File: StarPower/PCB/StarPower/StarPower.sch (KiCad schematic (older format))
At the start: 13 parts, among them SW1 SW_Push, U1 ATtiny25-20SSU, U2 SGM809, U3 PAM2804AAB010, Y1 32768 Hz

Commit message: Set more part footprints.
The microcontroller is now directly connected to the battery.
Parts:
- C1: footprint (none) -> Capacitor_SMD:C_1206_3216Metric_Pad1.42x1.75mm_HandSolder
- C2: renamed from C5; footprint (none) -> Capacitor_SMD:C_1206_3216Metric_Pad1.42x1.75mm_HandSolder
- C3: footprint (none) -> Capacitor_SMD:C_0805_2012Metric_Pad1.18x1.45mm_HandSolder
- C4: renamed from C2; footprint (none) -> Capacitor_SMD:C_0805_2012Metric_Pad1.18x1.45mm_HandSolder
- C5: renamed from C4; footprint (none) -> Capacitor_SMD:C_0805_2012Metric_Pad1.18x1.45mm_HandSolder
- U2: value SGM809 -> SGM809B-SXN3LG; footprint (none) -> Package_TO_SOT_SMD:SOT-23W_Handsoldering
- Y1: value 32768 Hz -> 32.768 kHz; footprint (none) -> Crystal:Crystal_SMD_SeikoEpson_MC146-4Pin_6.7x1.5mm_HandSoldering
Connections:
- net +2V8: no longer U1.8 (VCC)
- net +BATT: now also U1.8 (VCC)
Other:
- note added: "Iled ~~ 122 mA"
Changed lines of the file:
@@
-$EndComp
-$Comp
-L Device:Crystal Y1
-U 1 1 6369D0A6
-P 4600 5350
-F 0 "Y1" V 4350 5350 50  0000 C CNN
-F 1 "32768 Hz" V 4850 5350 50  0000 C CNN
-F 2 "" H 4600 5350 50  0001 C CNN
-F 3 "~" H 4600 5350 50  0001 C CNN
-	1    4600 5350
-	0    1    1    0
 $EndComp
 $Comp
@@
 F 0 "C3" H 5465 5546 50  0000 L CNN
 F 1 "C" H 5465 5455 50  0000 L CNN
-F 2 "" H 5388 5350 50  0001 C CNN
+F 2 "Capacitor_SMD:C_0805_2012Metric_Pad1.18x1.45mm_HandSolder" H 5388 5350 50  0001 C CNN
 F 3 "~" H 5350 5500 50  0001 C CNN
 	1    5350 5500
@@
 $EndComp
 $Comp
-L Device:C C2
+L Device:C C4
 U 1 1 6369DFE7
 P 5350 5200
-F 0 "C2" H 5465 5246 50  0000 L CNN
+F 0 "C4" H 5465 5246 50  0000 L CNN
 F 1 "C" H 5465 5155 50  0000 L CNN
-F 2 "" H 5388 5050 50  0001 C CNN
+F 2 "Capacitor_SMD:C_0805_2012Metric_Pad1.18x1.45mm_HandSolder" H 5388 5050 50  0001 C CNN
 F 3 "~" H 5350 5200 50  0001 C CNN
 	1    5350 5200
@@
 $EndComp
 $Comp
-L Device:C C5
+L Device:C C2
 U 1 1 636A08B3
 P 8250 3100
-F 0 "C5" H 8365 3146 50  0000 L CNN
+F 0 "C2" H 8365 3146 50  0000 L CNN
 F 1 "C1206C106K3PACTU" H 8365 3055 50  0000 L CNN
-F 2 "" H 8288 2950 50  0001 C CNN
+F 2 "Capacitor_SMD:C_1206_3216Metric_Pad1.42x1.75mm_HandSolder" H 8288 2950 50  0001 C CNN
 F 3 "~" H 8250 3100 50  0001 C CNN
 	1    8250 3100
@@
 $EndComp
 $Comp
-L Device:C C4
+L Device:C C5
 U 1 1 636A0DE7
 P 7750 3100
-F 0 "C4" H 7865 3146 50  0000 L CNN
+F 0 "C5" H 7865 3146 50  0000 L CNN
 F 1 "100 nF" H 7865 3055 50  0000 L CNN
-F 2 "" H 7788 2950 50  0001 C CNN
+F 2 "Capacitor_SMD:C_0805_2012Metric_Pad1.18x1.45mm_HandSolder" H 7788 2950 50  0001 C CNN
 F 3 "~" H 7750 3100 50  0001 C CNN
 	1    7750 3100
@@
 P 3100 3150
 F 0 "U2" H 2870 3196 50  0000 R CNN
-F 1 "SGM809" H 2870 3105 50  0000 R CNN
-F 2 "" H 2700 3300 50  0001 C CNN
+F 1 "SGM809B-SXN3LG" H 2870 3105 50  0000 R CNN
+F 2 "Package_TO_SOT_SMD:SOT-23W_Handsoldering" H 2700 3300 50  0001 C CNN
 F 3 "http://www.sg-micro.com/uploads/soft/20190626/1561528457.pdf" H 2800 3400 50  0001 C CNN
 	1    3100 3150
@@
 F 0 "C1" H 4665 3246 50  0000 L CNN
 F 1 "C1206C106K3PACTU" H 4665 3155 50  0000 L CNN
-F 2 "" H 4588 3050 50  0001 C CNN
+F 2 "Capacitor_SMD:C_1206_3216Metric_Pad1.42x1.75mm_HandSolder" H 4588 3050 50  0001 C CNN
 F 3 "~" H 4550 3200 50  0001 C CNN
 F 4 "±10 %; X5R" H 4550 3200 50  0001 C CNN "Characteristics"
@@
 	8250 3600 8250 3250
 Wire Wire Line
-	6850 3100 6450 3100
-Wire Wire Line
-	6450 3100 6450 2900
-Wire Wire Line
-	6450 2900 6000 2900
+	6850 3100 6100 3100
+Wire Wire Line
+	6100 3100 6100 2900
+Wire Wire Line
+	6100 2900 6000 2900
 Connection ~ 6850 3100
 Wire Wire Line
@@
 $EndComp
 Connection ~ 8250 2700
-$Comp
-L power:+2V8 #PWR0106
-U 1 1 636E305D
-P 2800 4650
-F 0 "#PWR0106" H 2800 4500 50  0001 C CNN
-F 1 "+2V8" H 2815 4823 50  0000 C CNN
-F 2 "" H 2800 4650 50  0001 C CNN
-F 3 "" H 2800 4650 50  0001 C CNN
-	1    2800 4650
-	1    0    0    -1
-$EndComp
 Wire Wire Line
 	2800 4650 2800 4700
@@
 Text Notes 7250 3350 0    50   ~ 0
 0.82 Ω
+$Comp
+L power:+BATT #PWR0106
+U 1 1 636EEFD2
+P 2800 4650
+F 0 "#PWR0106" H 2800 4500 50  0001 C CNN
+F 1 "+BATT" H 2815 4823 50  0000 C CNN
+F 2 "" H 2800 4650 50  0001 C CNN
+F 3 "" H 2800 4650 50  0001 C CNN
+	1    2800 4650
+	1    0    0    -1
+$EndComp
+$Comp
+L Device:Crystal Y1
+U 1 1 6369D0A6
+P 4600 5350
+F 0 "Y1" V 4350 5350 50  0000 C CNN
+F 1 "32.768 kHz" V 4850 5350 50  0000 C CNN
+F 2 "Crystal:Crystal_SMD_SeikoEpson_MC146-4Pin_6.7x1.5mm_HandSoldering" H 4600 5350 50  0001 C CNN
+F 3 "~" H 4600 5350 50  0001 C CNN
+	1    4600 5350
+	0    1    1    0
+$EndComp
+Text Notes 7000 3100 0    50   ~ 0
+Iled ~~ 122 mA
 $EndSCHEMATC

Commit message: Add mounting holes and the correct footprint for the push button.
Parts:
- added H1, H2: MountingHole, MountingHole:MountingHole_3.5mm, symbol Mechanical:MountingHole
- added H3: MountingHole, MountingHole:MountingHole_2.5mm, symbol Mechanical:MountingHole
- SW1: value SW_Push -> TL3301; footprint (none) -> mibe:SW_SPST_TL3301
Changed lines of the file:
@@
 P 4000 5000
 F 0 "SW1" H 4000 5285 50  0000 C CNN
-F 1 "SW_Push" H 4000 5194 50  0000 C CNN
-F 2 "" H 4000 5200 50  0001 C CNN
+F 1 "TL3301" H 4000 5194 50  0000 C CNN
+F 2 "mibe:SW_SPST_TL3301" H 4000 5200 50  0001 C CNN
 F 3 "~" H 4000 5200 50  0001 C CNN
 	1    4000 5000
@@
 Text Notes 7000 3100 0    50   ~ 0
 Iled ~~ 122 mA
+$Comp
+L Mechanical:MountingHole H1
+U 1 1 6372BC7B
+P 7700 6000
+F 0 "H1" H 7800 6046 50  0000 L CNN
+F 1 "MountingHole" H 7800 5955 50  0000 L CNN
+F 2 "MountingHole:MountingHole_3.5mm" H 7700 6000 50  0001 C CNN
+F 3 "~" H 7700 6000 50  0001 C CNN
+	1    7700 6000
+	1    0    0    -1
+$EndComp
+$Comp
+L Mechanical:MountingHole H2
+U 1 1 6372C182
+P 8500 6000
+F 0 "H2" H 8600 6046 50  0000 L CNN
+F 1 "MountingHole" H 8600 5955 50  0000 L CNN
+F 2 "MountingHole:MountingHole_3.5mm" H 8500 6000 50  0001 C CNN
+F 3 "~" H 8500 6000 50  0001 C CNN
+	1    8500 6000
+	1    0    0    -1
+$EndComp
+$Comp
+L Mechanical:MountingHole H3
+U 1 1 6372C56E
+P 9300 6000
+F 0 "H3" H 9400 6046 50  0000 L CNN
+F 1 "MountingHole" H 9400 5955 50  0000 L CNN
+F 2 "MountingHole:MountingHole_2.5mm" H 9300 6000 50  0001 C CNN
+F 3 "~" H 9300 6000 50  0001 C CNN
+	1    9300 6000
+	1    0    0    -1
+$EndComp
 $EndSCHEMATC

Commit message: Named most nets.
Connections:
- net SW: now reaches L1.1, U3.3 (SW)
- net FB: now reaches D1.1 (K), R1.1, U3.5 (FB)
- net XTAL1: now reaches C4.2, U1.2 (XTAL1/PB3), Y1.1
- net XTAL2: now reaches C3.2, U1.3 (XTAL2/PB4), Y1.2
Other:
- moved on the sheet: L1
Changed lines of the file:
@@
-$EndComp
-$Comp
-L Device:L L1
-U 1 1 6369E4E0
-P 6450 2700
-F 0 "L1" V 6640 2700 50  0000 C CNN
-F 1 "SRU1038-150Y" V 6549 2700 50  0000 C CNN
-F 2 "Inductor_SMD:L_Bourns-SRU1028_10.0x10.0mm" H 6450 2700 50  0001 C CNN
-F 3 "~" H 6450 2700 50  0001 C CNN
-F 4 "ESR as low as possible" H 6450 2700 50  0001 C CNN "Characteristics"
-	1    6450 2700
-	0    -1   -1   0
 $EndComp
 $Comp
@@
 	0    -1   -1   0
 $EndComp
-Text Notes 6350 2800 0    50   ~ 0
+Text Notes 6450 2800 0    50   ~ 0
 15 µH
 $Comp
@@
 	3000 3600 2400 3600
 Connection ~ 3000 3600
-Wire Wire Line
-	6300 2700 6000 2700
 Text GLabel 3650 3150 2    50   Output ~ 0
 RESET
@@
 Wire Wire Line
 	6850 2750 6850 2700
-Wire Wire Line
-	6850 2700 6600 2700
 Wire Wire Line
 	6850 3600 7750 3600
@@
 	1    0    0    -1
 $EndComp
+Text Label 4100 5400 0    50   ~ 0
+XTAL2
+Text Label 4100 5300 0    50   ~ 0
+XTAL1
+$Comp
+L Device:L L1
+U 1 1 6369E4E0
+P 6550 2700
+F 0 "L1" V 6740 2700 50  0000 C CNN
+F 1 "SRU1038-150Y" V 6649 2700 50  0000 C CNN
+F 2 "Inductor_SMD:L_Bourns-SRU1028_10.0x10.0mm" H 6550 2700 50  0001 C CNN
+F 3 "~" H 6550 2700 50  0001 C CNN
+F 4 "ESR as low as possible" H 6550 2700 50  0001 C CNN "Characteristics"
+	1    6550 2700
+	0    -1   -1   0
+$EndComp
+Wire Wire Line
+	6400 2700 6000 2700
+Wire Wire Line
+	6850 2700 6700 2700
+Text Label 6050 2700 0    50   ~ 0
+SW
+Text Label 6150 3100 0    50   ~ 0
+FB
 $EndSCHEMATC

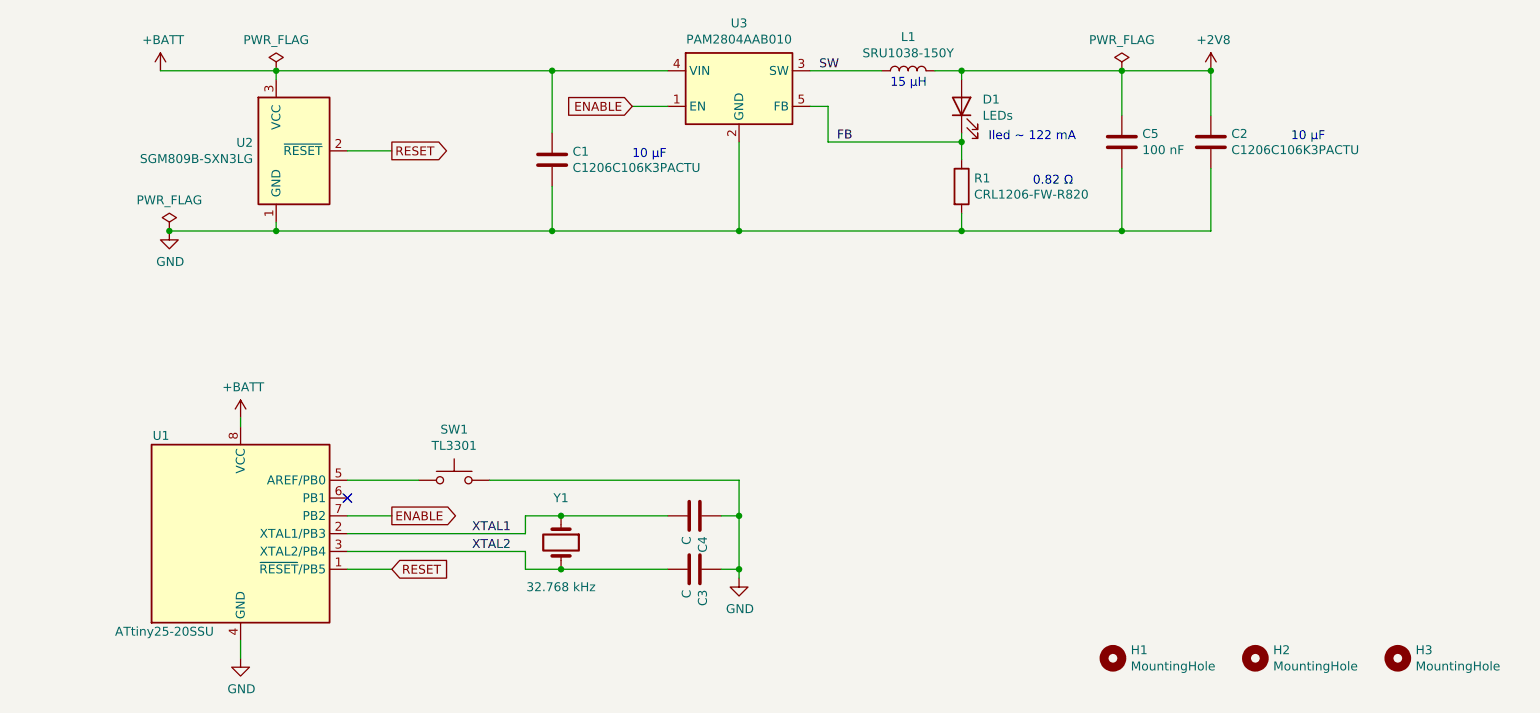
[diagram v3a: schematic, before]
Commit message: All components are placed, the traces are still missing.
The schematic has some changes:
- Y1 rotated to better fit placement on board
- C5 is now to +BATT instead of +2V8
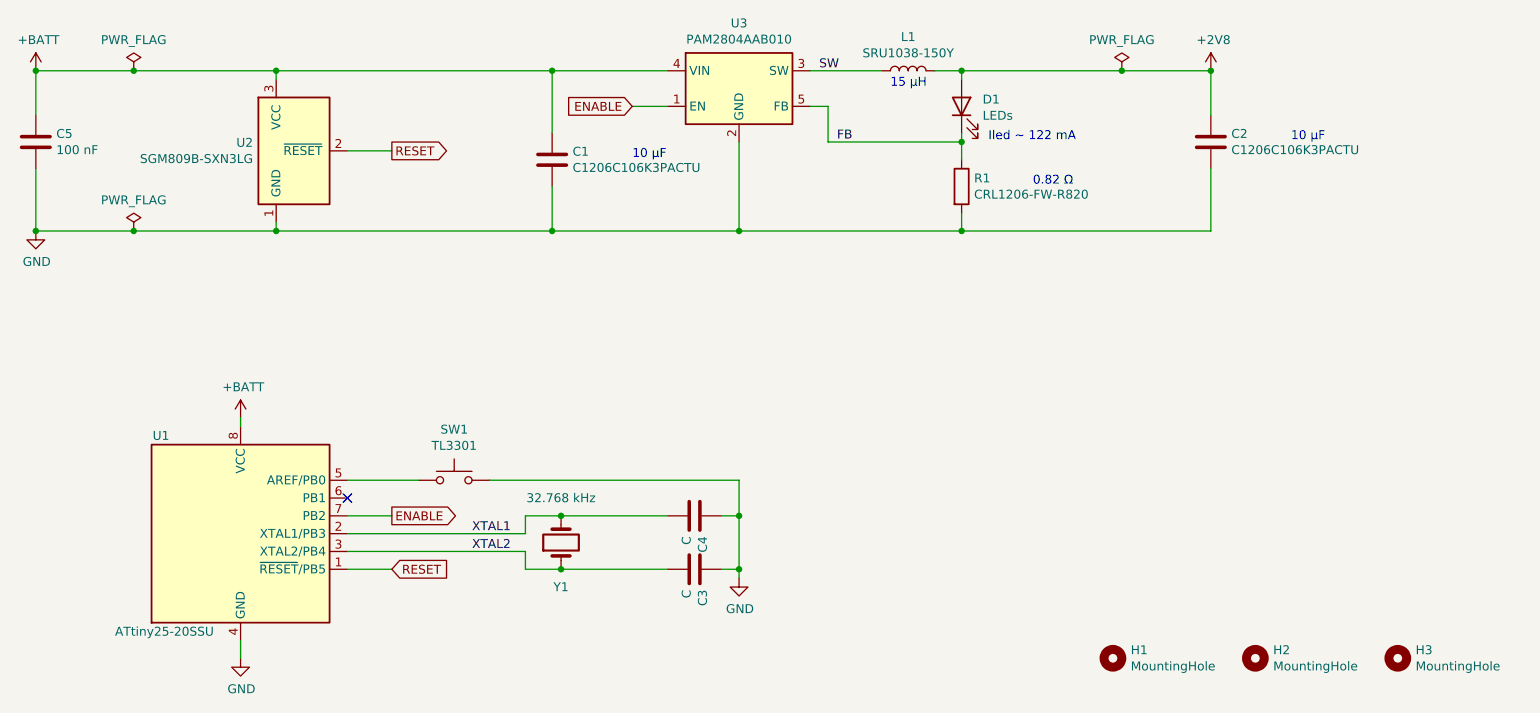
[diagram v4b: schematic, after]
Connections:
- net +2V8: no longer C5.1
- net +BATT: now also C5.1
- net XTAL1: now also Y1.2; no longer Y1.1
- net XTAL2: now also Y1.1; no longer Y1.2
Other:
- moved on the sheet: C5
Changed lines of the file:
@@
 L Device:C C5
 U 1 1 636A0DE7
-P 7750 3100
-F 0 "C5" H 7865 3146 50  0000 L CNN
-F 1 "100 nF" H 7865 3055 50  0000 L CNN
-F 2 "Capacitor_SMD:C_0805_2012Metric_Pad1.18x1.45mm_HandSolder" H 7788 2950 50  0001 C CNN
-F 3 "~" H 7750 3100 50  0001 C CNN
-	1    7750 3100
+P 1650 3100
+F 0 "C5" H 1765 3146 50  0000 L CNN
+F 1 "100 nF" H 1765 3055 50  0000 L CNN
+F 2 "Capacitor_SMD:C_0805_2012Metric_Pad1.18x1.45mm_HandSolder" H 1688 2950 50  0001 C CNN
+F 3 "~" H 1650 3100 50  0001 C CNN
+	1    1650 3100
 	1    0    0    -1
 $EndComp
@@
 L power:+BATT #PWR0102
 U 1 1 636B99F8
-P 2350 2700
-F 0 "#PWR0102" H 2350 2550 50  0001 C CNN
-F 1 "+BATT" H 2365 2873 50  0000 C CNN
-F 2 "" H 2350 2700 50  0001 C CNN
-F 3 "" H 2350 2700 50  0001 C CNN
-	1    2350 2700
-	1    0    0    -1
-$EndComp
-Wire Wire Line
-	2350 2700 3000 2700
+P 1650 2700
+F 0 "#PWR0102" H 1650 2550 50  0001 C CNN
+F 1 "+BATT" H 1665 2873 50  0000 C CNN
+F 2 "" H 1650 2700 50  0001 C CNN
+F 3 "" H 1650 2700 50  0001 C CNN
+	1    1650 2700
+	1    0    0    -1
+$EndComp
+Wire Wire Line
+	1650 2700 2200 2700
 Connection ~ 3000 2700
 $Comp
 L power:GND #PWR0103
 U 1 1 636BA4A7
-P 2400 3600
-F 0 "#PWR0103" H 2400 3350 50  0001 C CNN
-F 1 "GND" H 2405 3427 50  0000 C CNN
-F 2 "" H 2400 3600 50  0001 C CNN
-F 3 "" H 2400 3600 50  0001 C CNN
-	1    2400 3600
-	1    0    0    -1
-$EndComp
-Wire Wire Line
-	3000 3600 2400 3600
-Connection ~ 3000 3600
+P 1650 3600
+F 0 "#PWR0103" H 1650 3350 50  0001 C CNN
+F 1 "GND" H 1655 3427 50  0000 C CNN
+F 2 "" H 1650 3600 50  0001 C CNN
+F 3 "" H 1650 3600 50  0001 C CNN
+	1    1650 3600
+	1    0    0    -1
+$EndComp
 Text GLabel 3650 3150 2    50   Output ~ 0
 RESET
@@
 	3400 5500 3650 5500
 Wire Wire Line
-	4600 5500 4400 5500
-Wire Wire Line
 	4400 5500 4400 5400
 Wire Wire Line
 	4400 5400 3400 5400
 Wire Wire Line
-	4600 5200 4400 5200
-Wire Wire Line
 	4400 5200 4400 5300
 Wire Wire Line
 	4400 5300 3400 5300
-Wire Wire Line
-	5200 5200 4600 5200
-Wire Wire Line
-	4600 5500 5200 5500
 $Comp
 L power:GND #PWR0104
@@
 	6850 2750 6850 2700
 Wire Wire Line
-	6850 3600 7750 3600
-Wire Wire Line
 	8250 3600 8250 3250
 Wire Wire Line
@@
 Wire Wire Line
 	2800 6000 2800 5900
-Wire Wire Line
-	7750 2950 7750 2700
 Connection ~ 7750 2700
 Wire Wire Line
 	7750 2700 6850 2700
-Wire Wire Line
-	7750 3250 7750 3600
-Connection ~ 7750 3600
-Wire Wire Line
-	7750 3600 8250 3600
 Text Notes 8700 3100 0    50   ~ 0
 10 µF
@@
 L power:PWR_FLAG #FLG0102
 U 1 1 636E7652
-P 3000 2700
-F 0 "#FLG0102" H 3000 2775 50  0001 C CNN
-F 1 "PWR_FLAG" H 3000 2873 50  0000 C CNN
-F 2 "" H 3000 2700 50  0001 C CNN
-F 3 "~" H 3000 2700 50  0001 C CNN
-	1    3000 2700
-	1    0    0    -1
-$EndComp
-Connection ~ 4600 5500
-Connection ~ 4600 5200
+P 2200 2700
+F 0 "#FLG0102" H 2200 2775 50  0001 C CNN
+F 1 "PWR_FLAG" H 2200 2873 50  0000 C CNN
+F 2 "" H 2200 2700 50  0001 C CNN
+F 3 "~" H 2200 2700 50  0001 C CNN
+	1    2200 2700
+	1    0    0    -1
+$EndComp
 $Comp
 L power:PWR_FLAG #FLG0103
 U 1 1 636ECB08
-P 2400 3600
-F 0 "#FLG0103" H 2400 3675 50  0001 C CNN
-F 1 "PWR_FLAG" H 2400 3773 50  0000 C CNN
-F 2 "" H 2400 3600 50  0001 C CNN
-F 3 "~" H 2400 3600 50  0001 C CNN
-	1    2400 3600
-	1    0    0    -1
-$EndComp
-Connection ~ 2400 3600
+P 2200 3600
+F 0 "#FLG0103" H 2200 3675 50  0001 C CNN
+F 1 "PWR_FLAG" H 2200 3773 50  0000 C CNN
+F 2 "" H 2200 3600 50  0001 C CNN
+F 3 "~" H 2200 3600 50  0001 C CNN
+	1    2200 3600
+	1    0    0    -1
+$EndComp
+Connection ~ 1650 3600
 Connection ~ 5600 5500
 Wire Wire Line
@@
 F 3 "~" H 4600 5350 50  0001 C CNN
 	1    4600 5350
-	0    1    1    0
+	0    -1   -1   0
 $EndComp
 Text Notes 7000 3100 0    50   ~ 0
@@
 Text Label 6150 3100 0    50   ~ 0
 FB
+Wire Wire Line
+	6850 3600 8250 3600
+Wire Wire Line
+	1650 3600 2200 3600
+Connection ~ 3000 3600
+Wire Wire Line
+	1650 2700 1650 2950
+Connection ~ 1650 2700
+Wire Wire Line
+	1650 3600 1650 3250
+Connection ~ 2200 2700
+Wire Wire Line
+	2200 2700 3000 2700
+Connection ~ 2200 3600
+Wire Wire Line
+	2200 3600 3000 3600
+Wire Wire Line
+	4400 5500 4600 5500
+Wire Wire Line
+	4400 5200 4600 5200
+Connection ~ 4600 5500
+Wire Wire Line
+	4600 5500 5200 5500
+Connection ~ 4600 5200
+Wire Wire Line
+	4600 5200 5200 5200
 $EndSCHEMATC

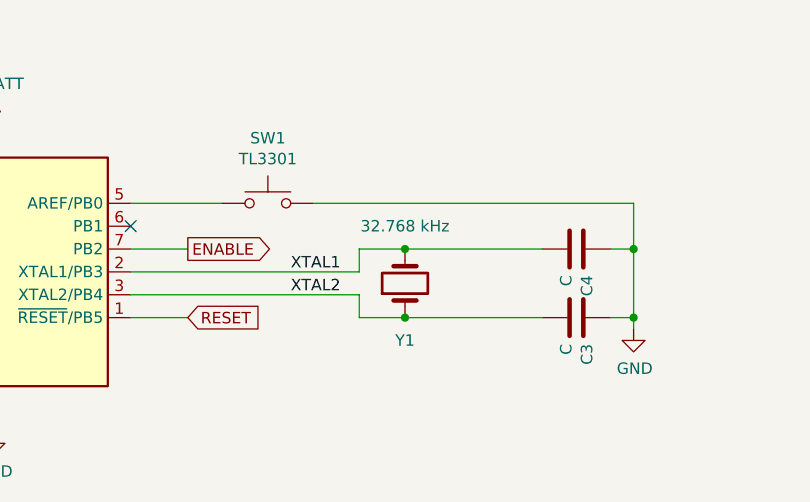
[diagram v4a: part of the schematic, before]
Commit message: Bugifx: The crystal footprint had the wrong pin mapping.
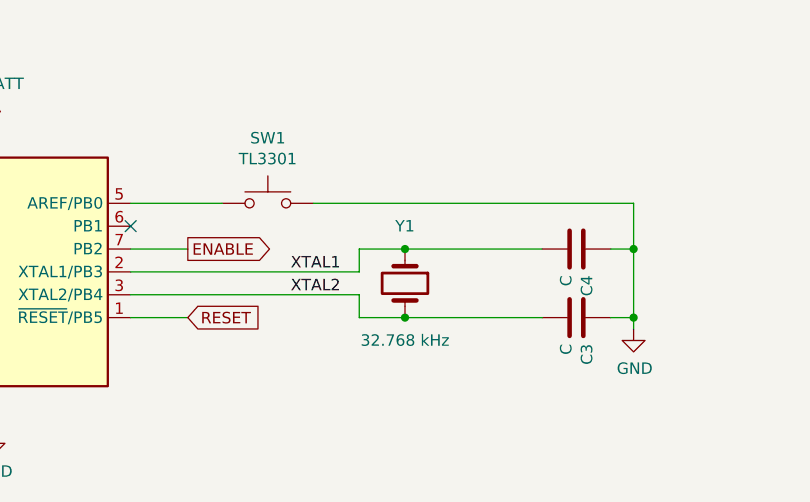
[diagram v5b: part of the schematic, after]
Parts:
- Y1: footprint Crystal:Crystal_SMD_SeikoEpson_MC146-4Pin_6.7x1.5mm_HandSoldering -> mibe:Crystal_SMD_Qantek_QTP7-4Pin_6.9x1.4mm_HandSoldering
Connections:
- net XTAL1: now also Y1.1; no longer Y1.2
- net XTAL2: now also Y1.2; no longer Y1.1
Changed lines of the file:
@@
 F 0 "Y1" V 4350 5350 50  0000 C CNN
 F 1 "32.768 kHz" V 4850 5350 50  0000 C CNN
-F 2 "Crystal:Crystal_SMD_SeikoEpson_MC146-4Pin_6.7x1.5mm_HandSoldering" H 4600 5350 50  0001 C CNN
+F 2 "mibe:Crystal_SMD_Qantek_QTP7-4Pin_6.9x1.4mm_HandSoldering" H 4600 5350 50  0001 C CNN
 F 3 "~" H 4600 5350 50  0001 C CNN
 	1    4600 5350
-	0    -1   -1   0
+	0    1    1    0
 $EndComp
 Text Notes 7000 3100 0    50   ~ 0
@@
 Wire Wire Line
 	4400 5200 4600 5200
+Connection ~ 4600 5200
+Wire Wire Line
+	4600 5200 5200 5200
 Connection ~ 4600 5500
 Wire Wire Line
 	4600 5500 5200 5500
-Connection ~ 4600 5200
-Wire Wire Line
-	4600 5200 5200 5200
 $EndSCHEMATC
